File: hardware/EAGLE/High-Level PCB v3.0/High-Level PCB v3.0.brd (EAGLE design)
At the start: 160 x 100 mm, 58 parts, among them IC1 MCP2551, IC2 DS8921, IC3 DS8921, J1 Optical Mouse, J2 RaspπUart, J8 DB9 Plug, J9 CAN Output, U1 COMPASS, U2 LLSHIFTER, U3 GPS, X1 Vehicle control, X2 RJ45-8L-B, X4 RJ45-8L-B

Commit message: Started board layout
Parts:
- moved U$3 176.8 mm to (99.5, 78.2), turned to 180 degrees
- moved U$1 165.1 mm to (58.8, 22.6), turned to 90 degrees
- moved U2 163.1 mm to (49.4, 2.17), turned to 90 degrees
- moved J8 140.9 mm to (25.6, 70.8)
- moved U1 137.6 mm to (34.6, 51.0), turned to 180 degrees
- moved J9 132.9 mm to (4.79, 67.6), turned to 270 degrees
- moved U$2 120.8 mm to (70.0, 60.7), turned to 180 degrees
- moved TP15 112.0 mm to (-113.0, 65.4)
- moved TP14 110.4 mm to (-108.2, 88.1)
- moved X4 105.2 mm to (51.4, 74.7), turned to 180 degrees
- moved X2 102.0 mm to (69.5, 74.7), turned to 180 degrees
- moved X1 91.7 mm to (7.71, 26.7), turned to 270 degrees
- moved MCU2 59.6 mm to (42.1, 36.5)
- moved U3 59.1 mm to (97.2, 20.9)
- moved IC1 19.2 mm to (-81.4, 109.4)
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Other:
- board size 160 x 100 mm -> 99.9 x 80.5 mm

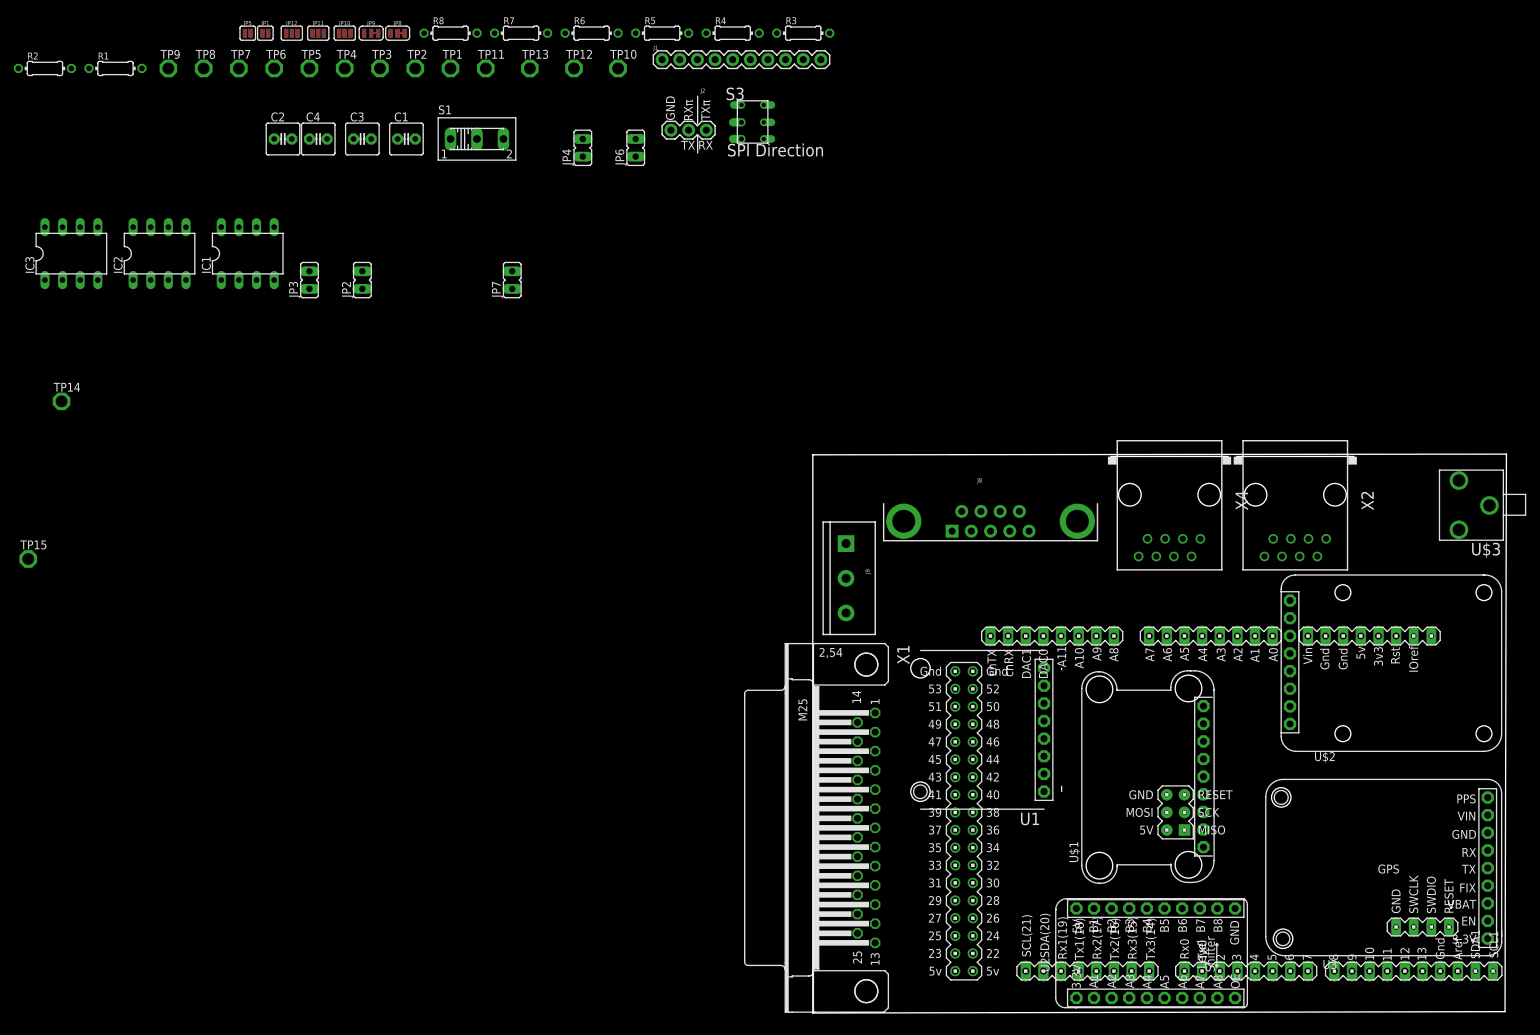
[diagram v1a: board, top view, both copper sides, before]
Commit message: 100% autoroute success
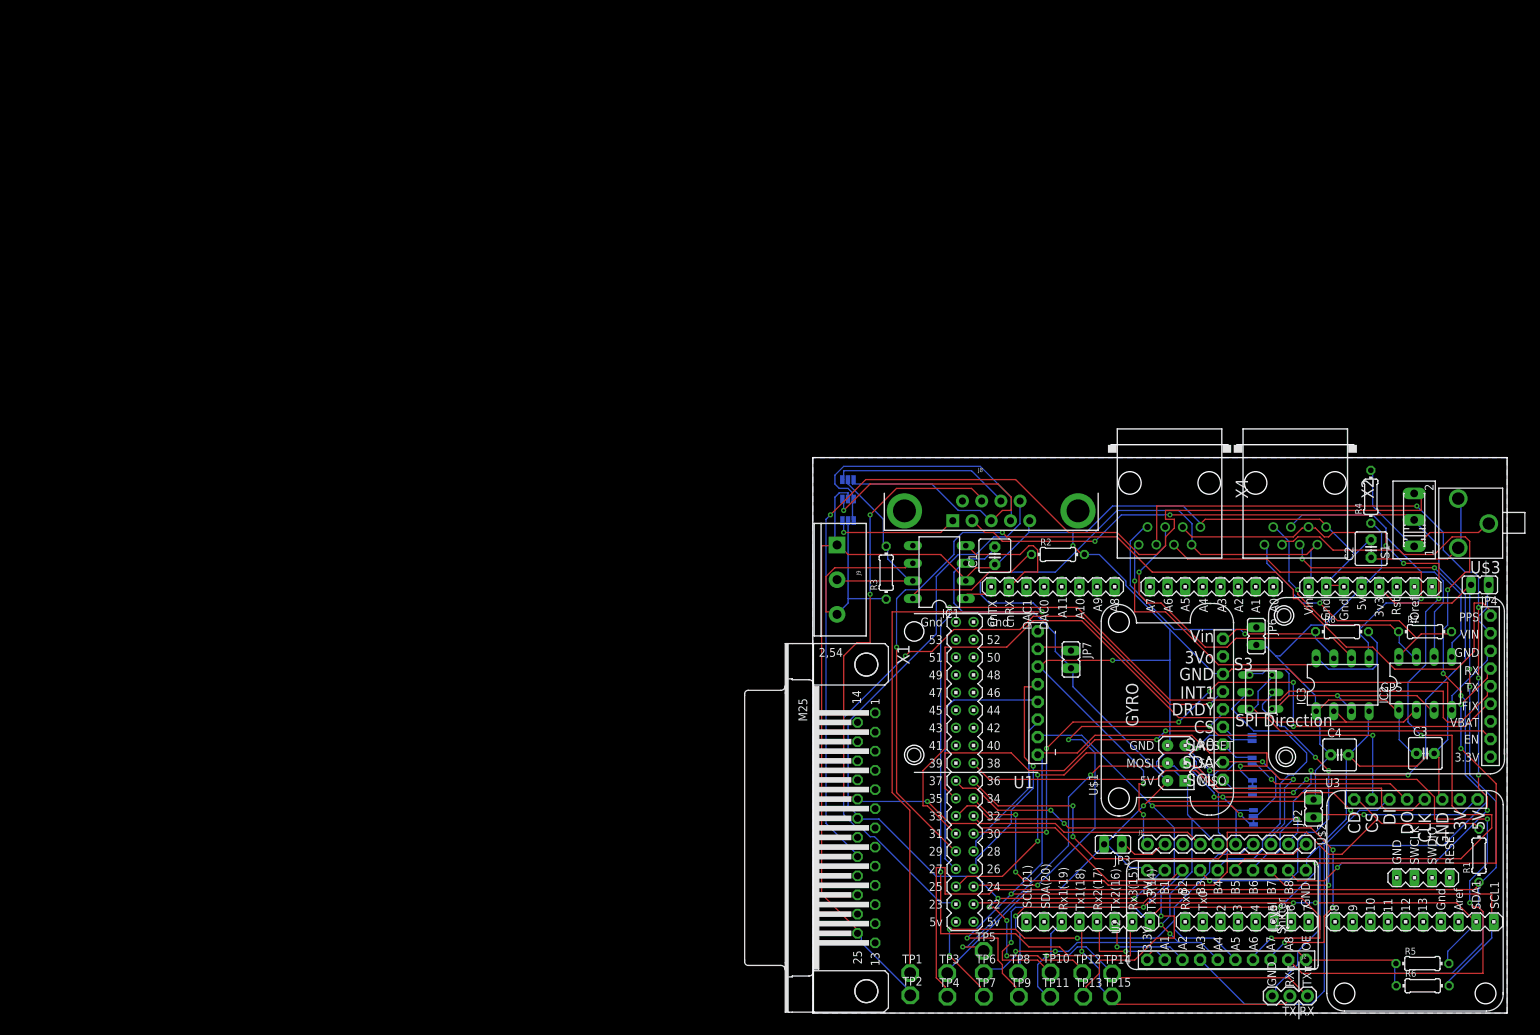
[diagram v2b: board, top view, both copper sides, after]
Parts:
- moved R1 226.8 mm to (96.0, 22.7), turned to 90 degrees
- moved IC3 193.3 mm to (76.3, 47.3)
- moved IC2 192.5 mm to (88.2, 47.5)
- moved R6 182.1 mm to (87.8, 3.93)
- moved TP9 181.3 mm to (29.7, 2.35)
- moved C3 176.8 mm to (88.2, 37.4)
- moved JP5 176.7 mm to (63.3, 39.6), flipped to the bottom, turned to 270 degrees
- moved JP1 176.6 mm to (63.3, 36.4), flipped to the bottom, turned to 270 degrees
- moved TP8 175.3 mm to (29.6, 5.75)
- moved R5 173.0 mm to (87.8, 7.13)
- moved TP14 172.3 mm to (43.1, 5.70)
- moved C4 171.8 mm to (75.9, 37.2)
- moved TP7 171.4 mm to (24.6, 2.35)
- moved JP9 170.0 mm to (63.5, 28.2), flipped to the bottom, turned to 270 degrees
- moved TP15 168.3 mm to (43.1, 2.40)
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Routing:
- net GND: track 0.00 -> 412.5 mm, vias 0 -> 4
- net +3V3: track 0.00 -> 227.5 mm, vias 0 -> 2
- net +5V: track 0.00 -> 208.4 mm, vias 0 -> 1
- net GPS_TX: track 0.00 -> 182.5 mm, vias 0 -> 3
- net SCL1: track 0.00 -> 174.6 mm, vias 0 -> 3
- net N$6: track 0.00 -> 153.6 mm, vias 0 -> 1
- net VIN: track 0.00 -> 151.0 mm, vias 0 -> 1
- net PPS: track 0.00 -> 148.8 mm, vias 0 -> 2
- net C2_RX: track 0.00 -> 147.8 mm, vias 0 -> 4
- net MOSI: track 0.00 -> 143.4 mm, vias 0 -> 5
- net CLICK: track 0.00 -> 142.7 mm, vias 0 -> 4
- net SDA1: track 0.00 -> 138.6 mm, vias 0 -> 6
- net SCK: track 0.00 -> 136.0 mm, vias 0 -> 3
- net CS_C5_REAR: track 0.00 -> 135.1 mm, vias 0 -> 4
- net C2_TX: track 0.00 -> 132.1 mm, vias 0 -> 5
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- added copper zone on layer 16, net GND
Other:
- board size 99.9 x 80.5 mm -> 100 x 80 mm

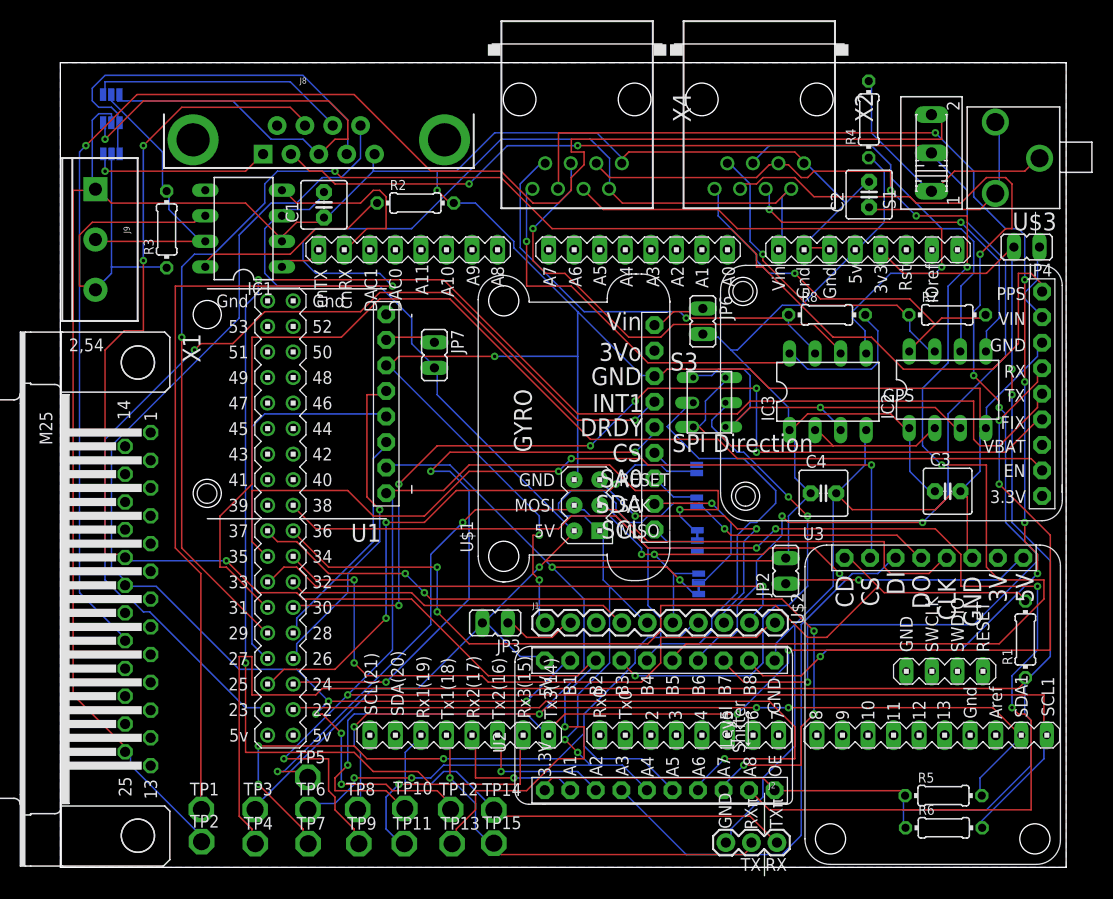
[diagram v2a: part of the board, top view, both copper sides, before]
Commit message: Moved files around
Current PCB files are moved one level up
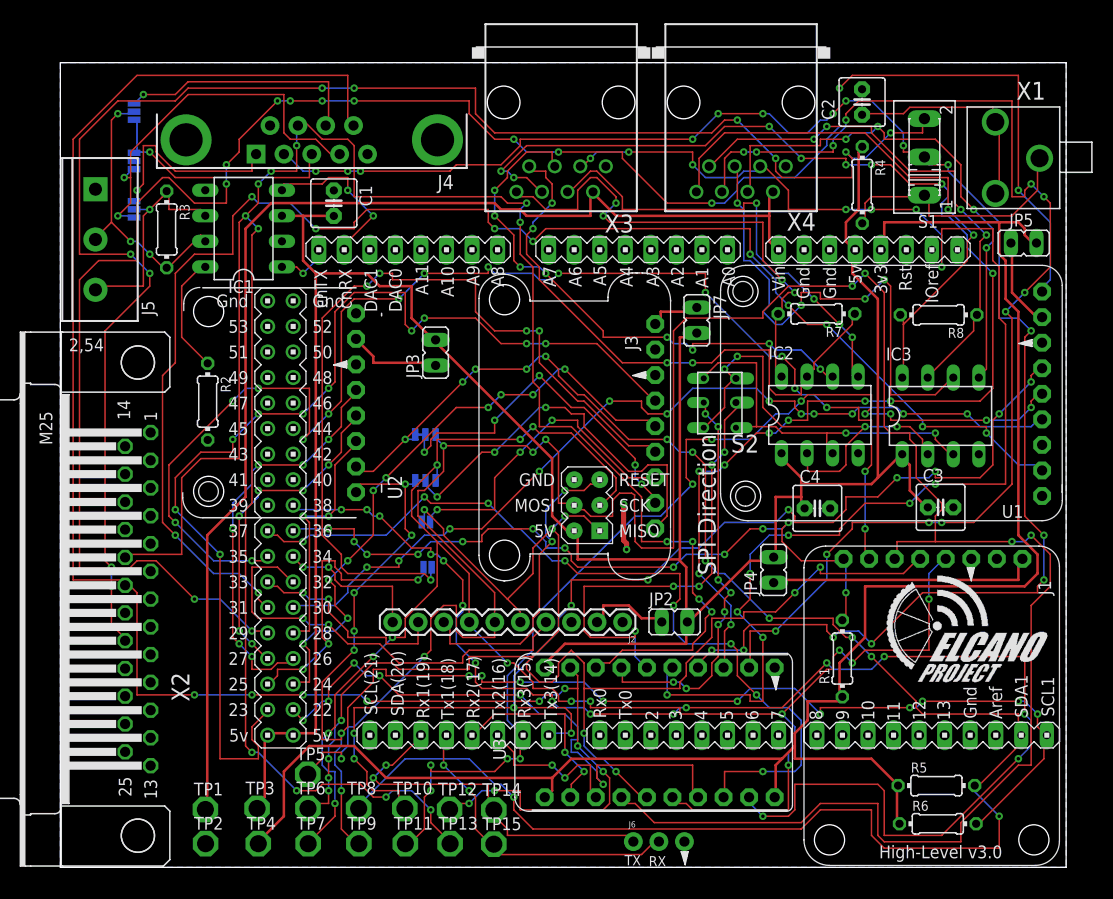
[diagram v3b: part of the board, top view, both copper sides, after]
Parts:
- removed J8: DB9 Plug, SparkFun-Connectors:DB9_MALE
- removed S3: SPI Direction, ELCano_Footprints:DPDT
- removed U$1: Gyro, ELCano_Footprints:ELGYRO
- removed U$2: Micro-SD, ELCano_Footprints:ELSDCARD
- removed U$3: (no value), ELCano_Footprints:2.5MMJACK
- added J3: Gyro, ELCano_Footprints:ELGYRO
- added J4: DB9 Plug, SparkFun-Connectors:DB9_MALE
- added J6: RaspπUart, ELCano_Footprints:1X03
- added S2: SPI Direction, ELCano_Footprints:DPDT
- added X3: Front Sonar, con-tycoelectronics:RJ45-NO-SHIELD
- J1: value Optical Mouse -> Micro-SD; device SparkFun-Connectors:1X10 -> ELCano_Footprints:ELSDCARD
- J2: value RaspπUart -> Optical Mouse; device tx_rxRasp:1X03 -> SparkFun-Connectors:1X10
- JP2: value MicroSD Power -> Mouse Power
- JP3: value Mouse Power -> Compass Power
- JP4: value GPS Power -> MicroSD Power
- JP5: value (none) -> GPS Power; device SparkFun-Jumpers:SMT-JUMPER_2_NO_SILK -> jumper:JP1
- JP6: value Gyro Power -> (none); device jumper:JP1 -> SparkFun-Jumpers:SMT-JUMPER_2_NO_SILK
- JP7: value Compass Power -> Gyro Power
- U1: value COMPASS -> GPS; device ELCOMPASS:ELCOMPASS -> ELCano_Footprints:ELGPS
- U2: value LLSHIFTER -> COMPASS; device ELSHIFTER:ELSHIFTER -> ELCano_Footprints:ELCOMPASS
- U3: value GPS -> LLSHIFTER; device ELGPS:ELGPS -> ELCano_Footprints:ELSHIFTER
- X1: value Vehicle control -> (none); device con-subd:M25H -> ELCano_Footprints:2.5MMJACK
- X2: value RJ45-8L-B -> Vehicle control; device con-tycoelectronics:RJ45-NO-SHIELD -> con-subd:M25H
- X4: value RJ45-8L-B -> Rear Sonar
- moved X1 103.9 mm to (99.4, 75.6), turned to 180 degrees
- moved X2 79.3 mm to (7.71, 26.7), turned to 270 degrees
- moved U1 64.6 mm to (97.6, 47.1)
- moved U2 56.6 mm to (30.7, 56.4), turned to 180 degrees
- moved J1 45.4 mm to (86.6, 0.20), turned to 90 degrees
- moved U3 42.8 mm to (72.8, 12.2), turned to 90 degrees
- moved JP4 40.8 mm to (70.9, 29.6), turned to 0 degrees
- moved JP5 39.5 mm to (95.8, 62.1), flipped to the top
- moved JP6 36.7 mm to (36.5, 29.8), flipped to the bottom, turned to 0 degrees
- moved JP9 31.0 mm to (36.3, 43.0), turned to 0 degrees
- moved R2 28.6 mm to (14.7, 46.3), turned to 270 degrees
- moved JP8 27.7 mm to (36.3, 38.5), turned to 0 degrees
- moved JP3 27.5 mm to (37.3, 51.2), turned to 0 degrees
- moved JP1 27.0 mm to (36.4, 34.3), turned to 0 degrees
- moved JP7 26.3 mm to (63.3, 54.4)
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- renumbered J9 to J5, MCU2 to MCU1
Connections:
- net +3V3: now also JP5.2, U3.1, U3.10; no longer JP4.2, U2.1, U2.10
- net +5V: now also JP4.2, MCU1.5V_A, MCU1.5V_B, U3.11; no longer JP6.2, U2.11
- net C2_RX: now also J4.8, U3.13, X2.18; no longer J8.8, U2.13, X1.18
- net C2_TX: now also J4.6, U3.12, X2.19; no longer J8.6, U2.12, X1.19
- net CARD_DETECT: now also J1.8; no longer U$2.8
- net CLICK: now also J4.4, U3.17; no longer J8.4, U2.17
- net CS_C5_FRONT: now also U3.8; no longer U2.8
- net CS_C5_FRONT_5V: now also U3.18, X3.6; no longer U2.18, X2.6
- net CS_C5_REAR: now also U3.9; no longer U2.9
- net CS_C5_REAR_5V: now also U3.19; no longer U2.19
- net CS_GYRO: now also JP6.2; no longer JP5.2
- net CS_MOUSE: now also J2.4; no longer J1.4
- net CS_SD: now also J1.7; no longer U$2.7
- net DRDY_C: now also U2.4; no longer U1.4
- net DRDY_G: now also J3.5; no longer U$1.5
- net EN: now also U1.8; no longer U3.8
- net FIX: now also U1.6; no longer U3.6
- net GND: now also J1.3, J2.1, J3.3, J4.1, J6.3, MCU1.GND1, MCU1.GND_A, MCU1.GND_B, U2.3, U3.20, X2.25, X3.1; no longer J1.1, J2.3, J8.1, U$1.3, U$2.3, U2.20, U3.3, X1.25, X2.1
- net GPS_RX: now also U1.4; no longer U3.4
- net GPS_TX: now also U1.5; no longer U3.5
- net I1: now also U2.5; no longer U1.5
- net I2: now also U2.6; no longer U1.6
- net INT1: now also J3.4; no longer U$1.4
- net LED: now also J2.10; no longer J1.10
- net MISO: now also J2.5, U3.5; no longer U$2.5, U2.5
- net MISO+: now also X3.5; no longer X2.5
- net MISO-: now also X3.4; no longer X2.4
- net MISO_5V: now also S2.5, U3.15; no longer S3.5, U2.15
- net MOSI: now also J2.6, U3.4; no longer U$2.6, U2.4
- net MOSI+: now also X3.8; no longer X2.8
- net MOSI-: now also X3.7; no longer X2.7
- net MOSI_5V: now also S2.2, U3.14; no longer S3.2, U2.14
- net N$1: now also X1.2, X1.3; no longer U$3.2, U$3.3
- net N$10: now also J1.1, JP4.1; no longer JP2.1, U$2.1
- net N$11: now also J4.3; no longer J8.3
- net N$12: now also U3.7; no longer U2.7
- net N$13: now also J2.2, JP2.1; no longer J1.2, JP3.1
- net N$14: now also JP5.1, U1.2; no longer JP4.1, U3.2
- net N$15: now also J4.5; no longer J8.5
- net N$16: now also J4.7; no longer J8.7
- net N$18: now also J4.2; no longer J8.2
- net N$19: now also J3.6, JP6.1; no longer JP5.1, U$1.6
- net N$2: now also S2.1, S2.6; no longer S3.1, S3.6
- net N$20: now also J3.7; no longer U$1.7
- net N$21: now also J3.8; no longer U$1.8
- net N$22: now also J3.9; no longer U$1.9
- net N$3: now also S2.3, S2.4; no longer S3.3, S3.4
- net N$4: now also U3.3; no longer U2.3
- net N$5: now also U3.2; no longer U2.2
- net N$6: now also X2.21; no longer X1.21
- net N$7: now also X1.1; no longer U$3.1
- net N$8: now also JP3.1, U2.2; no longer JP7.1, U1.2
- net N$9: now also J3.1, JP7.1; no longer JP6.1, U$1.1
- net NPD: now also J2.9; no longer J1.9
- net PPS: now also U1.1; no longer U3.1
- net RPI_RX: now also J6.2; no longer J2.2
- net RPI_TX: now also J6.1; no longer J2.1
- net RST: now also J2.8; no longer J1.8
- net SCK: now also J1.4, J2.7, U3.6; no longer J1.7, U$2.4, U2.6
- net SCK_5V: now also U3.16, X3.3; no longer U2.16, X2.3
- net SCL1: now also U2.8; no longer U1.8
- net SDA1: now also U2.7; no longer U1.7
- net VIN: now also X3.2; no longer X2.2
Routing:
- net GND: track 412.5 -> 4.62 mm, vias 4 -> 2
- net MOSI: track 143.4 -> 259.6 mm, vias 5 -> 9
- net C2_RX: track 147.8 -> 235.0 mm, vias 4 -> 15
- net GPS_TX: track 182.5 -> 103.1 mm, vias 3 -> 11
- net N$19: track 4.69 -> 82.9 mm, vias 0 -> 5
- net CS_SD: track 81.8 -> 132.6 mm, vias 3 -> 16
- net PPS: track 148.8 -> 197.2 mm, vias 2 -> 13
- net +3V3: track 227.5 -> 180.1 mm, vias 2 -> 0
- net LED: track 61.8 -> 15.1 mm
- net SDA1: track 138.6 -> 184.0 mm, vias 6 -> 13
- net +5V: track 208.4 -> 251.5 mm, vias 1 -> 0
- net C2_TX: track 132.1 -> 175.1 mm, vias 5 -> 10
- net SCK: track 136.0 -> 172.6 mm, vias 3 -> 15
- net N$22: track 4.76 -> 39.1 mm, vias 0 -> 3
- net MISO: track 116.0 -> 149.9 mm, vias 5 -> 11
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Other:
- board text added: "CAN SELECT"
- board text added: "GYRO COM SELECT"
- board text added: "High-Level v3.0"
- board text added: "RX"
- board text added: "TX"
